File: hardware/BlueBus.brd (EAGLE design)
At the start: 90 x 60 mm, 141 parts, among them Q1 NMOSFET-BSS138K, Q2 PMOSFET-DMP32D4S, Q3 NMOSFET-BSS138K, X1 CRYSTAL-12MHZ

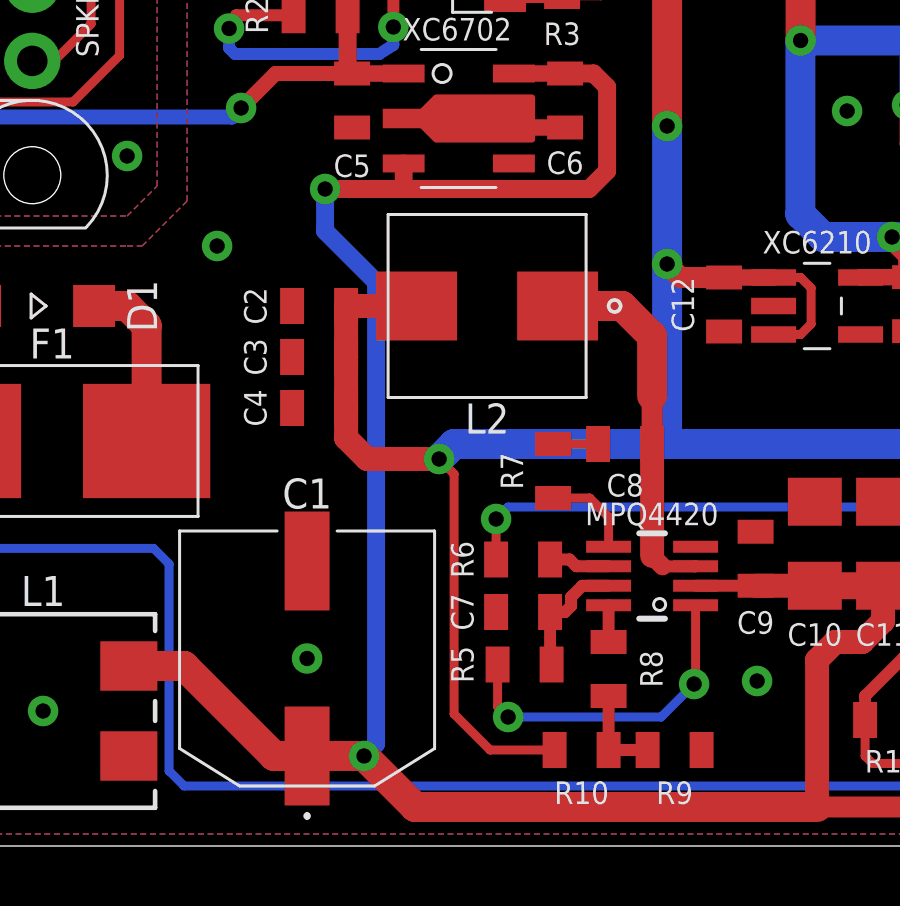
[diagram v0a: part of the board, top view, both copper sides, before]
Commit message: [IMP] harware: v1.5 updates * Replace L2 with MPL-SE5040-100 as other part is OOS * Replace C12 and C13 with 22uF capacitors * Replace 22uF capacitor part with one rated for 16v
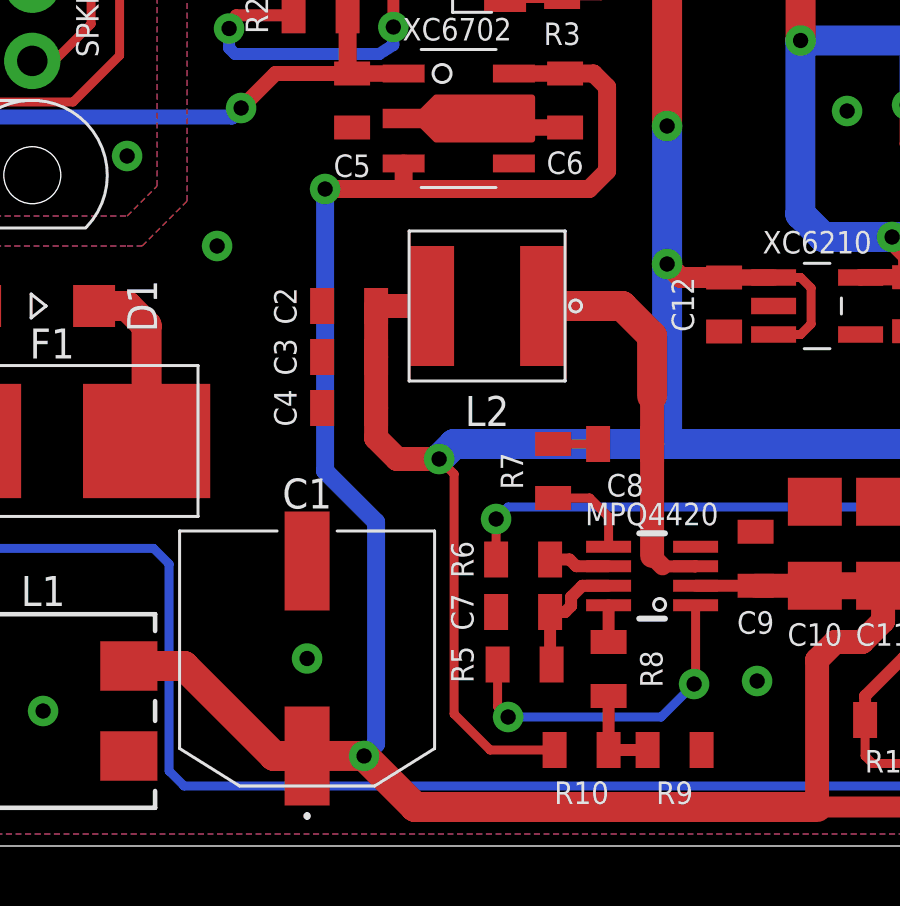
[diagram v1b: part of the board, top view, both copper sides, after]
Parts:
- C12, C13: value 1uF -> 22uF
- L2: value ETQ-P4M100KFN -> 10uH; device Passives:PCC-M0648M-LE -> Passives:MPL-SE5040
- moved C2 1.00 mm to (23.4, 18.0)
- moved C3 1.00 mm to (23.4, 16.3)
- moved C4 1.00 mm to (23.4, 14.6)
- turned L2 to 0 degrees
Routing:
- net 5V: track 206.0 -> 204.5 mm
- net 5VREG_SW: track 12.5 -> 13.0 mm
